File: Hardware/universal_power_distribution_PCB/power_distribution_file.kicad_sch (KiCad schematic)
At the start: 13 parts, among them J1 Screw_Terminal_01x02, U2 INA228

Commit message: Updated universal PCB
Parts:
- added C1, C10, C11, C12, C13, C14, C2, C5, C6, C7, C8, C9: C, symbol Device:C
- added D1, D2, D3, D4, D5, D6, D7: LED, symbol Device:LED
- added J2, J3, J4, J5, J6, J7: Screw_Terminal_01x02, symbol Connector:Screw_Terminal_01x02
- added L1, L2, L3, L4, L5: L, symbol Device:L
- added Q1, Q2, Q3, Q4, Q5: LMR51635XDDCR, SOT95P280X110-6N, symbol LMR51635XDDCR:LMR51635XDDCR
- added Q6: BSS84, Package_TO_SOT_SMD:SOT-23, symbol Transistor_FET:BSS84
- added R1, R13, R14, R15, R16, R17, R18, R19, R2, R20, R21, R22, R23, R24, R25, R26, R27, R28, R29, R4: 10k, symbol Device:R
- added R3: R_Shunt, symbol Device:R_Shunt
- added R30: 0R, symbol Device:R
- added R5, R6: R50, symbol Device:R
- added TP1: TestPoint, symbol Connector:TestPoint
- added U1: INA228, Package_SO:VSSOP-10_3x3mm_P0.5mm, symbol Sensor_Energy:INA228
- added U3: ACS711xEXLT-31AB, Sensor_Current:Allegro_QFN-12-10-1EP_3x3mm_P0.5mm, symbol Sensor_Current:ACS711xEXLT-31AB
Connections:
- net +42V: now also F2.1, C1.1, C11.1, C13.1, C5.1, C9.1, Q1.2 (EN), Q1.3 (VIN), Q2.2 (EN), Q2.3 (VIN), Q3.2 (EN), Q3.3 (VIN), Q4.2 (EN), Q4.3 (VIN), Q5.2 (EN), Q5.3 (VIN); no longer R7.4
- net +5V: now also C7.1, L5.2, Q6.3 (D), R14.2, R15.2, R16.2, R22.1, U1.6 (VS), U3.10 (VCC)
- net +MD_42V: now also D1.2 (A), J7.1 (Pin_1)
- net GND: now also C1.2, C11.2, C13.2, C5.2, C7.2, C9.2, J2.2 (Pin_2), J3.2 (Pin_2), J4.2 (Pin_2), J5.2 (Pin_2), J6.2 (Pin_2), J7.2 (Pin_2), Q1.4 (GND), Q2.4 (GND), Q3.4 (GND), Q4.4 (GND), Q5.4 (GND), R17.2, R19.2, R2.2, R21.2, R23.1, R24.1, R25.1, R26.1, R27.1, R28.1, R29.2, R4.2, U1.1 (A1), U1.2 (A0), U1.7 (GND), U3.3 (GND)
- net INA_SCL: now also R15.1, U1.5 (SCL)
- net INA_SDA: now also R14.1, U1.4 (SDA)
- net INA_alert: now also R16.1, U1.3 (~{Alert})
- net +S_42V renamed +24V
- net +24V: now also L1.2, R1.1; no longer F2.1
- new net: R3.3, R6.1
- new net: C6.2, R6.2, U1.9 (Vin-)
- new net: Q4.1 (FB), R19.1, R20.2
- new net: D4.1 (K), R26.2
- new net: C12.2, L4.1, Q4.5 (SW)
- new net: C12.1, Q4.6 (CB)
- new net: C6.1, R5.2, U1.10 (Vin+)
- new net: Q2.1 (FB), R13.2, R4.1
- new net: C2.1, Q1.6 (CB)
- new net: C2.2, L1.1, Q1.5 (SW)
- new net: R3.2, R5.1
- new net: C8.2, L2.1, Q2.5 (SW)
- new net: C10.2, L3.1, Q3.5 (SW)
- new net: Q6.1 (G), U3.4 (~{FAULT})
- new net: R30.1, U3.9 (VIOUT)
- new net: D3.1 (K), R25.2
- new net: D1.1 (K), R23.2
- new net: D5.1 (K), R27.2
- new net: D2.1 (K), R24.2
- new net: C8.1, Q2.6 (CB)
- new net: D7.1 (K), R29.1
- new net: C14.1, Q5.6 (CB)
- new net: C14.2, L5.1, Q5.5 (SW)
- new net: D7.2 (A), Q6.2 (S)
- new net: Q3.1 (FB), R17.1, R18.2
- new net: Q5.1 (FB), R21.1, R22.2
- new net: C10.1, Q3.6 (CB)
- new net: D6.1 (K), R28.2
- new net: Q1.1 (FB), R1.2, R2.1
- new net +12V: L4.2, R20.1
- new net +12V_out: D5.2 (A), J5.1 (Pin_1)
- new net +16V: L3.2, R18.1
- new net +16V_out: D4.2 (A), J4.1 (Pin_1)
- new net +19V: L2.2, R13.1, R3.1, TP1.1, U1.8 (Vbus)
- new net +19V_out: D3.2 (A), J3.1 (Pin_1), R3.4
- new net +24V_out: D2.2 (A), J2.1 (Pin_1), R7.4
- new net +5V_out: D6.2 (A), J6.1 (Pin_1)
- new net IP+: U3.1 (IP+)
- new net IP-: U3.2 (IP-)
- new net VIOUT: R30.2
- no-connect marks 0 -> 4
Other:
- note added: "3.5A Max"
- note added: "42 -> 12 DC/DC buck converter"
- note added: "42 -> 16 DC/DC buck converter"
- note added: "42 -> 19 DC/DC buck converter"
- note added: "42 -> 24 DC/DC buck converter"
- note added: "42 -> 5 DC/DC buck converter"
- note added: "Main Current sensor"
- note added: "Power LEDS"
- note added: "Voltage out connectors"
- company: (none) -> Lapin AMK
- title: (none) -> Power distribution pcb
- moved on the sheet: C3, C4, F1, F2, J1, R10, R11, R12, R7, R8, R9, TP2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

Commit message: finalized schematic 1
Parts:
- added C15, C16, C17, C18, C19, C20, C21, C22, C23, C24: C, symbol Device:C
- D1, D2, D3, D5, D6: footprint (none) -> LED_SMD:LED_0603_1608Metric_Pad1.05x0.95mm_HandSolder
- D4, R1, R10, R11, R12, R13, R14, R15, R16, R17, R18, R2, R21, R22, R29, R30, R4, R5, R6, R8, R9: footprint (none) -> Resistor_SMD:R_0603_1608Metric_Pad0.98x0.95mm_HandSolder
- R23: value 10k -> 4k; footprint (none) -> Resistor_SMD:R_0603_1608Metric_Pad0.98x0.95mm_HandSolder
- R24: value 10k -> 2.2k; footprint (none) -> Resistor_SMD:R_0603_1608Metric_Pad0.98x0.95mm_HandSolder
- R25: value 10k -> 1.8k; footprint (none) -> Resistor_SMD:R_0603_1608Metric_Pad0.98x0.95mm_HandSolder
- R26: value 10k -> 1.4k; footprint (none) -> Resistor_SMD:R_0603_1608Metric_Pad0.98x0.95mm_HandSolder
- R27: value 10k -> 1k; footprint (none) -> Resistor_SMD:R_0603_1608Metric_Pad0.98x0.95mm_HandSolder
- R28: value 10k -> 330; footprint (none) -> Resistor_SMD:R_0603_1608Metric_Pad0.98x0.95mm_HandSolder
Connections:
- net +12V is gone; now on net +12V_out: L4.2, R20.1
- net +16V is gone; now on net +16V_out: L3.2, R18.1
- net +5V_out is gone; now on net +5V: D6.2 (A), J6.1 (Pin_1)
- net +12V_out: now also C22.2
- net +16V_out: now also C21.2
- net +19V: now also C23.2
- net +24V: now also C16.2
- net +5V: now also C24.2
- net GND: now also C15.1, C16.1, C17.1, C18.1, C19.1, C20.1, C21.1, C22.1, C23.1, C24.1
- net at Q4.1 (FB), R19.1, R20.2: now also C19.2
- net at Q2.1 (FB), R13.2, R4.1: now also C20.2
- net at Q3.1 (FB), R17.1, R18.2: now also C18.2
- net at Q5.1 (FB), R21.1, R22.2: now also C17.2
- net at Q1.1 (FB), R1.2, R2.1: now also C15.2
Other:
- moved on the sheet: C1, C10, C11, C12, C13, C14, C2, C3, C4, C5, C6, C7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

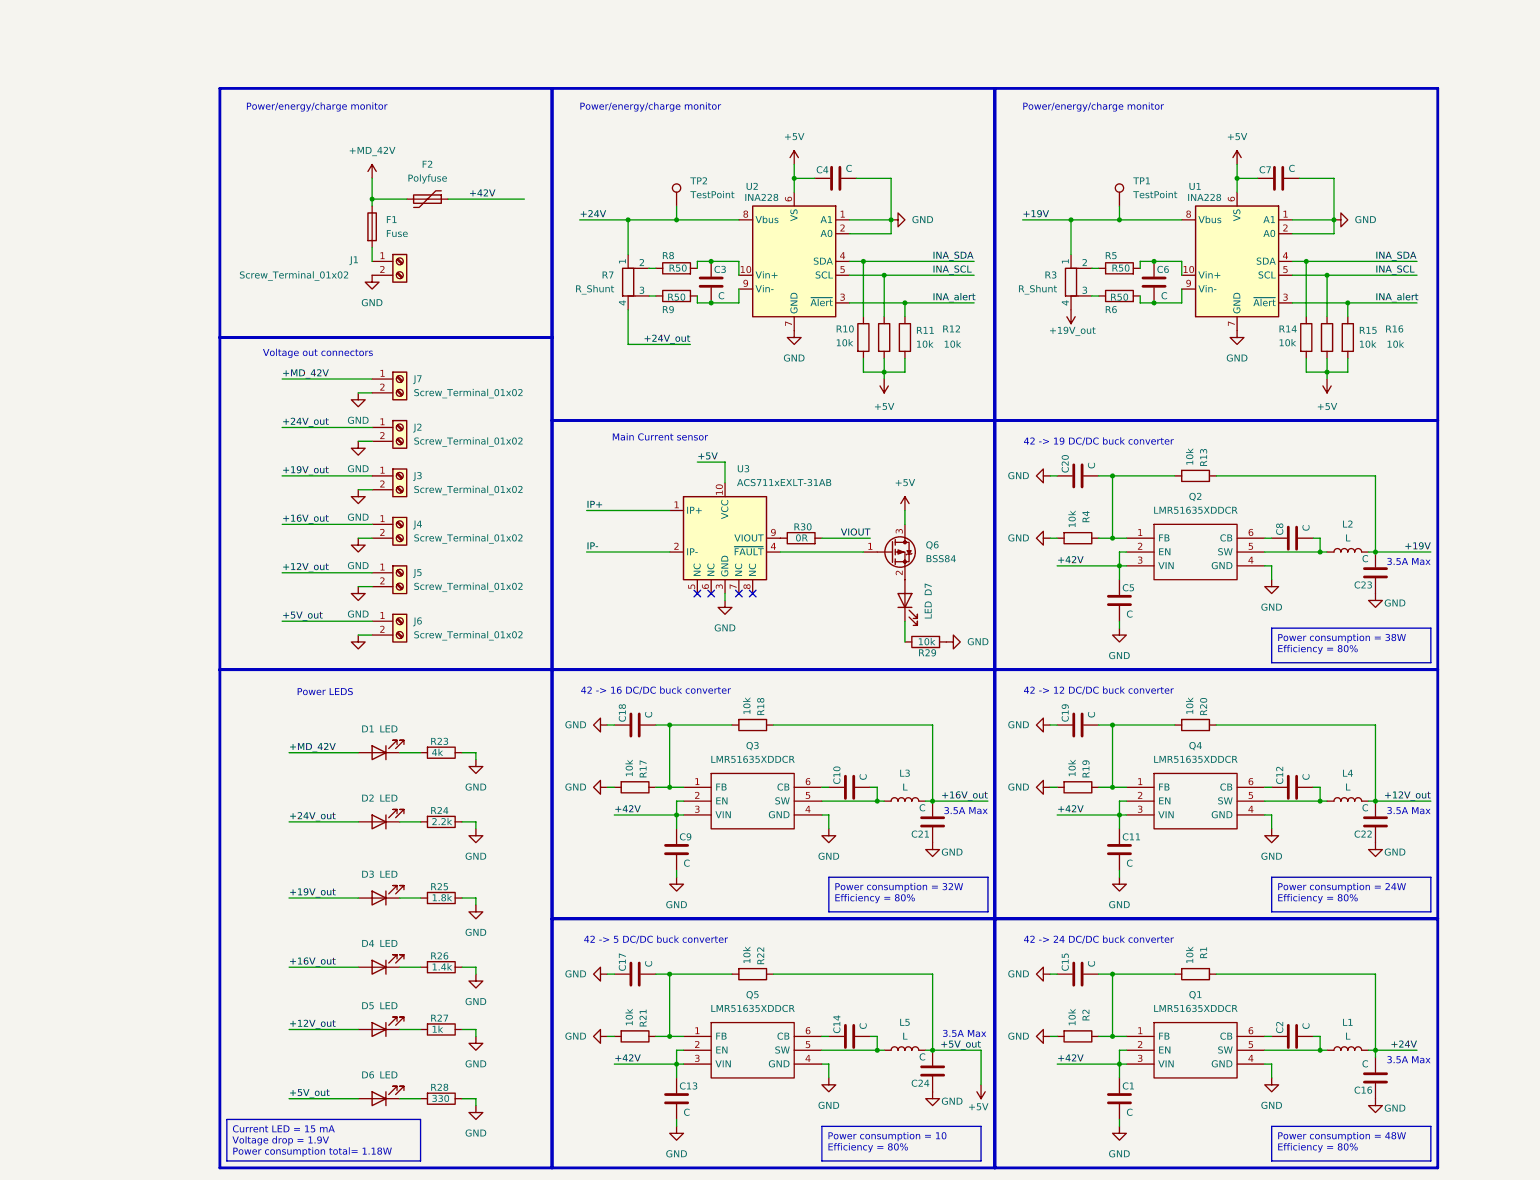
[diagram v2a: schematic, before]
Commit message: Updated pcb, added feedback resistors
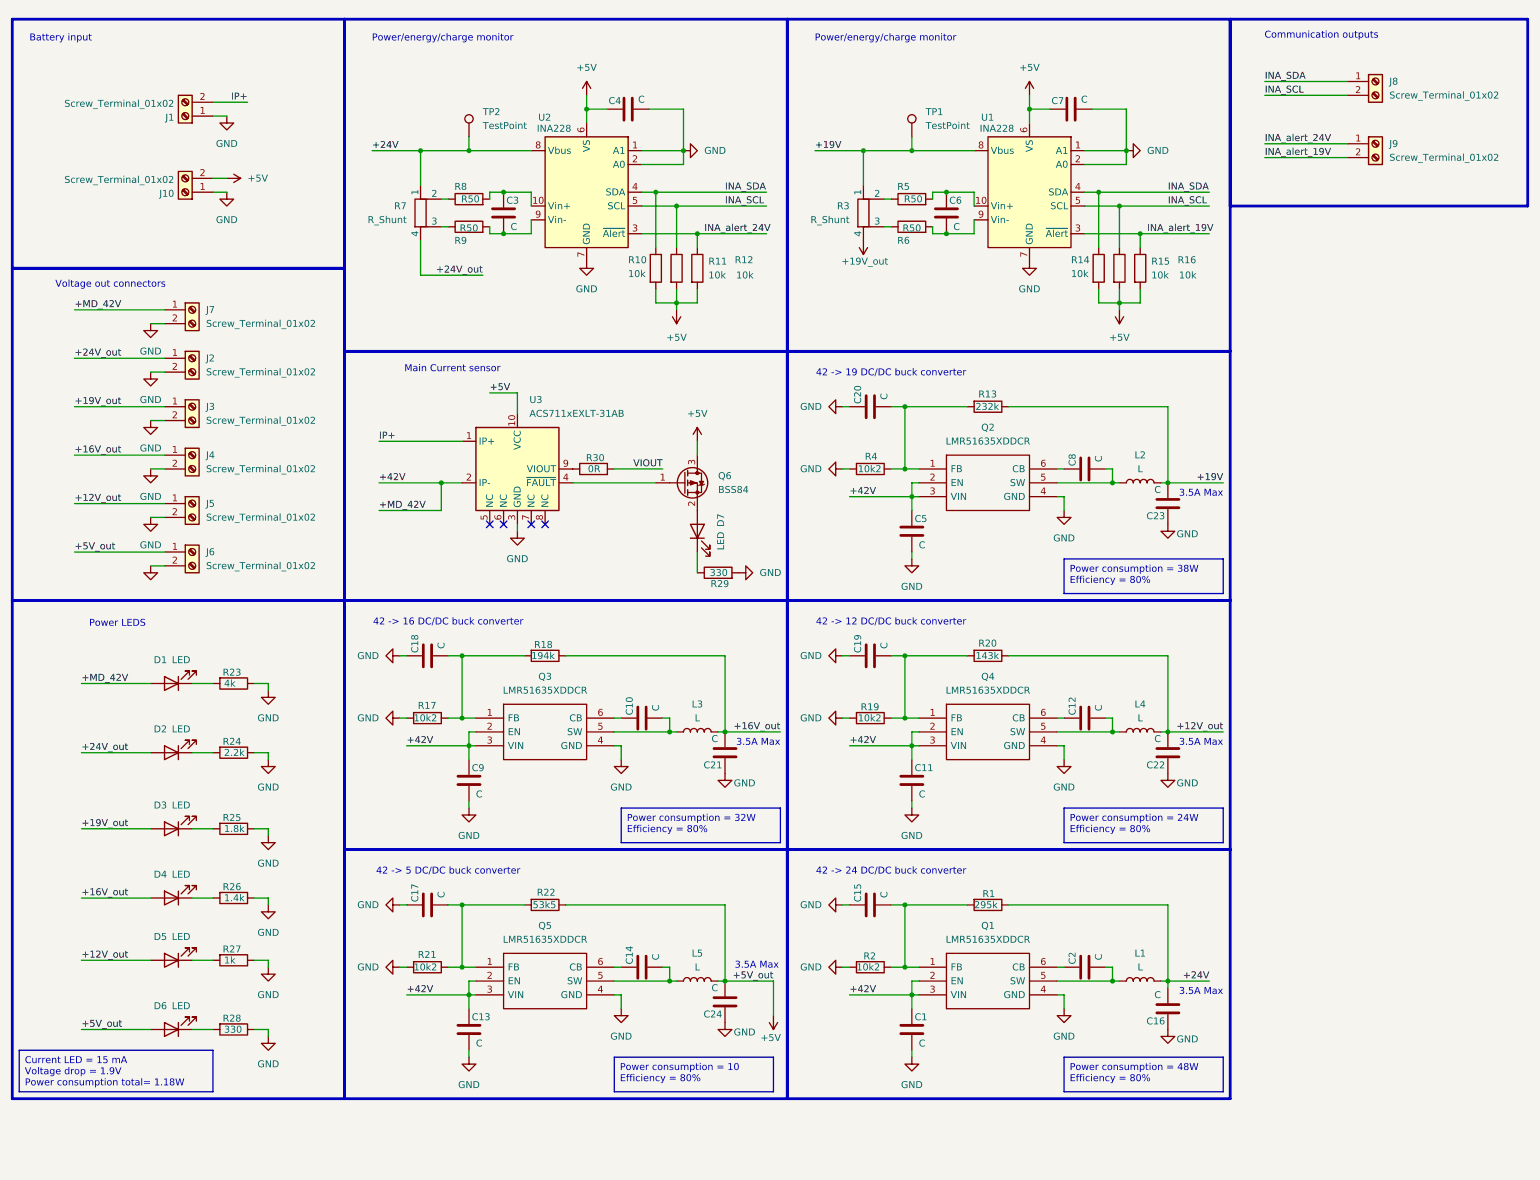
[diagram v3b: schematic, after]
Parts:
- removed F1: Fuse, Fuse:Fuse_Bourns_MF-RHT1300, symbol Device:Fuse
- removed F2: Polyfuse, symbol Device:Polyfuse
- added J10, J8, J9: Screw_Terminal_01x02, symbol Connector:Screw_Terminal_01x02
- R1: value 10k -> 295k
- R13: value 10k -> 232k
- R17, R19, R2, R21, R4: value 10k -> 10k2
- R18: value 10k -> 194k
- R20: value 10k -> 143k
- R22: value 10k -> 53k5
- R29: value 10k -> 330
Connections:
- net +MD_42V is gone; now on net +42V: D1.2 (A), J7.1 (Pin_1)
- net IP- is gone; now on net +42V: U3.2 (IP-)
- net +5V: now also J10.2 (Pin_2)
- net GND: now also J1.1 (Pin_1), J10.1 (Pin_1); no longer J1.2 (Pin_2)
- net INA_SCL: now also J8.2 (Pin_2)
- net INA_SDA: now also J8.1 (Pin_1)
- net IP+: now also J1.2 (Pin_2)
- net INA_alert renamed INA_alert_19V
- net INA_alert_19V: now also J9.2 (Pin_2); no longer R12.1, U2.3 (~{Alert})
- new net INA_alert_24V: J9.1 (Pin_1), R12.1, U2.3 (~{Alert})
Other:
- note added: "Battery input"
- note added: "Communication outputs"
- moved on the sheet: C1, C10, C11, C12, C13, C14, C15, C16, C17, C18, C19, C2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

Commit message: Restructured pcb
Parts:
- removed C3, C4, C6, C7: C, symbol Device:C
- removed D1, D2, D3, D5, D6: LED, LED_SMD:LED_0603_1608Metric_Pad1.05x0.95mm_HandSolder, symbol Device:LED
- removed D4: LED, Resistor_SMD:R_0603_1608Metric_Pad0.98x0.95mm_HandSolder, symbol Device:LED
- removed D7: LED, symbol Device:LED
- removed J1, J10, J2, J3, J4, J5, J6, J7, J8, J9: Screw_Terminal_01x02, symbol Connector:Screw_Terminal_01x02
- removed Q6: BSS84, Package_TO_SOT_SMD:SOT-23, symbol Transistor_FET:BSS84
- removed R10, R11, R12, R14, R15, R16: 10k, Resistor_SMD:R_0603_1608Metric_Pad0.98x0.95mm_HandSolder, symbol Device:R
- removed R23: 4k, Resistor_SMD:R_0603_1608Metric_Pad0.98x0.95mm_HandSolder, symbol Device:R
- removed R24: 2.2k, Resistor_SMD:R_0603_1608Metric_Pad0.98x0.95mm_HandSolder, symbol Device:R
- removed R25: 1.8k, Resistor_SMD:R_0603_1608Metric_Pad0.98x0.95mm_HandSolder, symbol Device:R
- removed R26: 1.4k, Resistor_SMD:R_0603_1608Metric_Pad0.98x0.95mm_HandSolder, symbol Device:R
- removed R27: 1k, Resistor_SMD:R_0603_1608Metric_Pad0.98x0.95mm_HandSolder, symbol Device:R
- removed R28, R29: 330, Resistor_SMD:R_0603_1608Metric_Pad0.98x0.95mm_HandSolder, symbol Device:R
- removed R3, R7: R_Shunt, symbol Device:R_Shunt
- removed R30: 0R, Resistor_SMD:R_0603_1608Metric_Pad0.98x0.95mm_HandSolder, symbol Device:R
- removed R5, R6, R8, R9: R50, Resistor_SMD:R_0603_1608Metric_Pad0.98x0.95mm_HandSolder, symbol Device:R
- removed TP1, TP2: TestPoint, symbol Connector:TestPoint
- removed U1, U2: INA228, Package_SO:VSSOP-10_3x3mm_P0.5mm, symbol Sensor_Energy:INA228
- removed U3: ACS711xEXLT-31AB, Sensor_Current:Allegro_QFN-12-10-1EP_3x3mm_P0.5mm, symbol Sensor_Current:ACS711xEXLT-31AB
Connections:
- no-connect marks 4 -> 0
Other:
- note removed: "Battery input"
- note removed: "Communication outputs"
- note removed: "Main Current sensor"
- note removed: "Power LEDS"
- note removed: "Power/energy/charge monitor"
- note removed: "Voltage out connectors"
- moved on the sheet: C1, C10, C11, C12, C13, C14, C15, C16, C17, C18, C19, C2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
